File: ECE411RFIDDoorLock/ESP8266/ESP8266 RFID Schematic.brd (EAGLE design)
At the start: 61 x 43.8 mm, 27 parts, among them M1 SERVO, Q3 DMG341, T1 600mA/40V, T2 600mA/40V, U3 AP2112-3.3, X1 ESP-12E, X4 20329

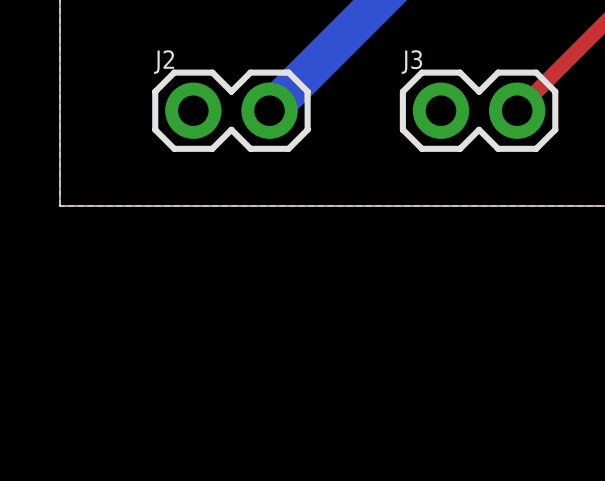
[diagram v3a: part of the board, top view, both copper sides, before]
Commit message: Added some missing component values
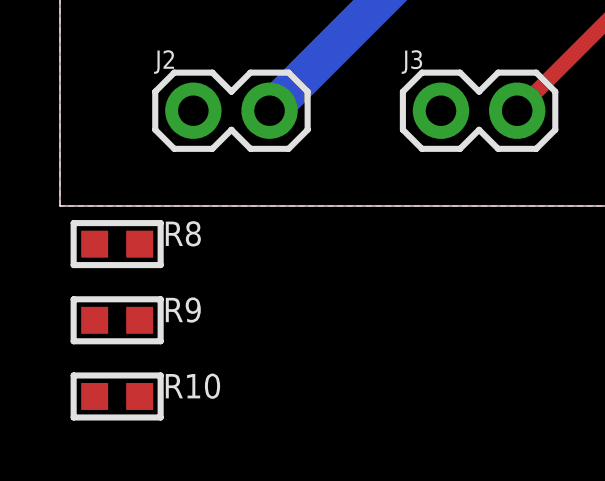
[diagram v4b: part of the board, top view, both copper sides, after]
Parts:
- added R10, R9: 10k, microbuilder:0603-MINI
- added R8: 4.7k, microbuilder:0603-MINI
- C1: value (none) -> 10µF
- C4: value (none) -> 1µF
- R2: value (none) -> 1k
- R3, R5, R6: value (none) -> 10k
- R4: value (none) -> 4.7k
- R7: value 10k -> 100k
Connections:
- net 3.3V: now also R10.2, R9.2
- net CH_PD: now also R9.1
- net GND: now also R8.1
- net GPIO15: now also R8.2
- net GPIO2: now also R10.1
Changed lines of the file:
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@@
 </autorouter>
 <elements>
-<element name="C1" library="microbuilder" package="0603-MINI" value="" x="12.7" y="22.86" smashed="yes" rot="R90">
+<element name="C1" library="microbuilder" package="0603-MINI" value="10µF" x="12.7" y="22.86" smashed="yes" rot="R90">
 <attribute name="NAME" x="12.7635" y="24.384" size="0.8128" layer="25" ratio="18" rot="R90"/>
 <attribute name="VALUE" x="13.335" y="24.384" size="0.4064" layer="27" ratio="10" rot="R90"/>
@@
 <attribute name="VALUE" x="10.795" y="24.384" size="0.4064" layer="27" ratio="10" rot="R90"/>
 </element>
-<element name="C4" library="microbuilder" package="0603-MINI" value="" x="4.445" y="26.67" smashed="yes" rot="R270">
+<element name="C4" library="microbuilder" package="0603-MINI" value="1µF" x="4.445" y="26.67" smashed="yes" rot="R270">
 <attribute name="NAME" x="4.3815" y="25.146" size="0.8128" layer="25" ratio="18" rot="R270"/>
 <attribute name="VALUE" x="3.81" y="25.146" size="0.4064" layer="27" ratio="10" rot="R270"/>
@@
 <attribute name="VALUE" x="13.335" y="20.574" size="0.4064" layer="27" ratio="10" rot="R90"/>
 </element>
-<element name="R2" library="microbuilder" package="0603-MINI" value="" x="11.43" y="35.56" smashed="yes" rot="R180">
+<element name="R2" library="microbuilder" package="0603-MINI" value="1k" x="11.43" y="35.56" smashed="yes" rot="R180">
 <attribute name="NAME" x="9.906" y="35.6235" size="0.8128" layer="25" ratio="18" rot="R180"/>
 <attribute name="VALUE" x="9.906" y="36.195" size="0.4064" layer="27" ratio="10" rot="R180"/>
 </element>
-<element name="R3" library="microbuilder" package="0603-MINI" value="" x="23.495" y="26.67" smashed="yes" rot="R270">
+<element name="R3" library="microbuilder" package="0603-MINI" value="10k" x="23.495" y="26.67" smashed="yes" rot="R270">
 <attribute name="NAME" x="23.4315" y="25.146" size="0.8128" layer="25" ratio="18" rot="R270"/>
 <attribute name="VALUE" x="22.86" y="25.146" size="0.4064" layer="27" ratio="10" rot="R270"/>
 </element>
-<element name="R4" library="microbuilder" package="0603-MINI" value="" x="20.955" y="22.225" smashed="yes" rot="R270">
+<element name="R4" library="microbuilder" package="0603-MINI" value="4.7k" x="20.955" y="22.225" smashed="yes" rot="R270">
 <attribute name="NAME" x="20.8915" y="20.701" size="0.8128" layer="25" ratio="18" rot="R270"/>
 <attribute name="VALUE" x="20.32" y="20.701" size="0.4064" layer="27" ratio="10" rot="R270"/>
 </element>
-<element name="R5" library="microbuilder" package="0603-MINI" value="" x="20.955" y="26.67" smashed="yes" rot="R90">
+<element name="R5" library="microbuilder" package="0603-MINI" value="10k" x="20.955" y="26.67" smashed="yes" rot="R90">
 <attribute name="NAME" x="21.0185" y="28.194" size="0.8128" layer="25" ratio="18" rot="R90"/>
 <attribute name="VALUE" x="21.59" y="28.194" size="0.4064" layer="27" ratio="10" rot="R90"/>
 </element>
-<element name="R6" library="microbuilder" package="0603-MINI" value="" x="17.145" y="31.115" smashed="yes" rot="R180">
+<element name="R6" library="microbuilder" package="0603-MINI" value="10k" x="17.145" y="31.115" smashed="yes" rot="R180">
 <attribute name="NAME" x="15.621" y="31.1785" size="0.8128" layer="25" ratio="18" rot="R180"/>
 <attribute name="VALUE" x="15.621" y="31.75" size="0.4064" layer="27" ratio="10" rot="R180"/>
 </element>
-<element name="R7" library="microbuilder" package="0603-MINI" value="10k" x="15.24" y="22.86" smashed="yes" rot="R270">
+<element name="R7" library="microbuilder" package="0603-MINI" value="100k" x="15.24" y="22.86" smashed="yes" rot="R270">
 <attribute name="NAME" x="15.1765" y="21.336" size="0.8128" layer="25" ratio="18" rot="R270"/>
 <attribute name="VALUE" x="14.605" y="21.336" size="0.4064" layer="27" ratio="10" rot="R270"/>
@@
 <attribute name="NAME" x="9.89" y="45.349" size="0.8128" layer="25" ratio="18" rot="R180"/>
 <attribute name="VALUE" x="9.89" y="45.907" size="0.4064" layer="27" ratio="10" rot="R180"/>
+</element>
+<element name="R8" library="microbuilder" package="0603-MINI" value="4.7k" x="1.905" y="-1.27" smashed="yes">
+<attribute name="NAME" x="3.429" y="-1.3335" size="0.8128" layer="25" ratio="18"/>
+<attribute name="VALUE" x="3.429" y="-1.905" size="0.4064" layer="27" ratio="10"/>
+</element>
+<element name="R9" library="microbuilder" package="0603-MINI" value="10k" x="1.905" y="-3.81" smashed="yes">
+<attribute name="NAME" x="3.429" y="-3.8735" size="0.8128" layer="25" ratio="18"/>
+<attribute name="VALUE" x="3.429" y="-4.445" size="0.4064" layer="27" ratio="10"/>
+</element>
+<element name="R10" library="microbuilder" package="0603-MINI" value="10k" x="1.905" y="-6.35" smashed="yes">
+<attribute name="NAME" x="3.429" y="-6.4135" size="0.8128" layer="25" ratio="18"/>
+<attribute name="VALUE" x="3.429" y="-6.985" size="0.4064" layer="27" ratio="10"/>
 </element>
 </elements>
@@
 <vertex x="0" y="0"/>
 </polygon>
-<wire x1="6.362" y1="41.497" x2="7.862" y2="41.497" width="0" layer="19" extent="1-1"/>
-<wire x1="5.812" y1="38.722" x2="6.362" y2="41.497" width="0" layer="19" extent="1-1"/>
+<contactref element="R8" pad="1"/>
+<wire x1="42.425" y1="20.345" x2="57.15" y2="33.655" width="0" layer="19" extent="1-1"/>
+<wire x1="25.4" y1="3.175" x2="32.385" y2="16.51" width="0" layer="19" extent="1-1"/>
+<wire x1="12.7" y1="3.175" x2="25.4" y2="3.175" width="0" layer="19" extent="1-1"/>
+<wire x1="4.445" y1="3.175" x2="12.7" y2="3.175" width="0" layer="19" extent="1-1"/>
+<wire x1="1.155" y1="-1.27" x2="4.445" y2="3.175" width="0" layer="19" extent="1-1"/>
+<wire x1="11.43" y1="17.145" x2="12.7" y2="3.175" width="0" layer="19" extent="1-1"/>
+<wire x1="10.16" y1="23.61" x2="10.1901" y2="17.145" width="0" layer="19" extent="1-1"/>
+<wire x1="12.7" y1="25.4" x2="10.16" y2="25.4" width="0" layer="19" extent="1-1"/>
+<wire x1="15.24" y1="25.4" x2="12.7" y2="25.4" width="0" layer="19" extent="1-1"/>
+<wire x1="7.62" y1="23.61" x2="10.16" y2="23.61" width="0" layer="19" extent="1-1"/>
+<wire x1="7.017" y1="30.595" x2="4.445" y2="25.92" width="0" layer="19" extent="1-1"/>
+<wire x1="4.572" y1="37.465" x2="5.715" y2="31.115" width="0" layer="19" extent="1-1"/>
+<wire x1="3.812" y1="38.597" x2="4.572" y2="37.465" width="0" layer="19" extent="1-1"/>
+<wire x1="6.362" y1="41.497" x2="5.812" y2="38.722" width="0" layer="19" extent="1-1"/>
+<wire x1="7.862" y1="41.497" x2="6.362" y2="41.497" width="0" layer="19" extent="1-1"/>
+<wire x1="3.512" y1="41.397" x2="3.812" y2="38.597" width="0" layer="19" extent="1-1"/>
+<wire x1="10.712" y1="41.397" x2="7.862" y2="41.497" width="0" layer="19" extent="1-1"/>
+<wire x1="10.412" y1="38.597" x2="10.712" y2="41.397" width="0" layer="19" extent="1-1"/>
+<wire x1="20.32" y1="41.91" x2="10.712" y2="41.397" width="0" layer="19" extent="1-1"/>
+<wire x1="23.209" y1="34.573" x2="23.209" y2="41.373" width="0" layer="19" extent="1-1"/>
 </signal>
 <signal name="N$9">
@@
 <wire x1="44.45" y1="22.345" x2="50.045" y2="22.345" width="0.508" layer="16"/>
 <wire x1="50.045" y1="22.345" x2="53.975" y2="18.415" width="0.508" layer="16"/>
+<contactref element="R8" pad="2"/>
+<wire x1="2.655" y1="-1.27" x2="30.48" y2="3.175" width="0" layer="19" extent="1-1"/>
 </signal>
 <signal name="GPIO0">
@@
 <wire x1="48.895" y1="24.765" x2="50.165" y2="26.035" width="0.508" layer="1"/>
 <wire x1="50.165" y1="26.035" x2="53.975" y2="26.035" width="0.508" layer="1"/>
+<contactref element="R10" pad="1"/>
+<wire x1="1.155" y1="-6.35" x2="42.425" y2="24.345" width="0" layer="19" extent="1-1"/>
 </signal>
 <signal name="GPIO5/SCL">
@@
 <wire x1="29.845" y1="30.353" x2="29.8704" y2="30.3784" width="0.508" layer="16"/>
 <wire x1="32.6287" y1="30.3784" x2="40.8239" y2="22.1832" width="0.508" layer="16"/>
+<contactref element="R9" pad="1"/>
+<wire x1="1.155" y1="-3.81" x2="27.425" y2="30.345" width="0" layer="19" extent="1-1"/>
 </signal>
 <signal name="USB_RX">
@@
 <contactref element="U1" pad="7"/>
 <contactref element="JP4" pad="15"/>
-<contactref element="U3" pad="5"/>
-<contactref element="C2" pad="1"/>
 <contactref element="C3" pad="1"/>
 <polygon width="0.2" layer="1">
@@
 <vertex x="0" y="0"/>
 </polygon>
+<contactref element="U3" pad="5"/>
+<contactref element="C2" pad="1"/>
+<contactref element="R9" pad="2"/>
+<contactref element="R10" pad="2"/>
+<wire x1="27.425" y1="20.345" x2="57.15" y2="38.735" width="0" layer="19" extent="1-1"/>
+<wire x1="23.495" y1="25.92" x2="27.425" y2="20.345" width="0" layer="19" extent="1-1"/>
+<wire x1="19.443" y1="19.05" x2="23.495" y2="25.92" width="0" layer="19" extent="1-1"/>
+<wire x1="10.16" y1="22.11" x2="19.443" y2="19.05" width="0" layer="19" extent="1-1"/>
+<wire x1="7.62" y1="22.11" x2="10.16" y2="22.11" width="0" layer="19" extent="1-1"/>
+<wire x1="7.767" y1="27.845" x2="7.62" y2="22.11" width="0" layer="19" extent="1-1"/>
+<wire x1="7.5899" y1="16.195" x2="7.62" y2="22.11" width="0" layer="19" extent="1-1"/>
+<wire x1="2.655" y1="-3.81" x2="7.5899" y2="16.195" width="0" layer="19" extent="1-1"/>
+<wire x1="2.655" y1="-6.35" x2="2.655" y2="-3.81" width="0" layer="19" extent="1-1"/>
+<wire x1="48.26" y1="3.175" x2="27.425" y2="20.345" width="0" layer="19" extent="1-1"/>
 </signal>
 <signal name="N$2">
